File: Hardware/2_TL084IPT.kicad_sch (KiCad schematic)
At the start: 34 parts

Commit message: after merge dev
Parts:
- gave numbers to parts that had none: 30

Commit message: add R0603 footprint
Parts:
- C18: footprint (none) -> IVS_FOOTPRINTS:C0603
- R42, R43, R44, R45, R46, R47, R48, R49, R50, R51, R52, R53, R54, R55, R56, R57: footprint (none) -> IVS_FOOTPRINTS:R0603
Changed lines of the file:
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@@
       (effects (font (size 1.27 1.27)) (justify left))
     )
-    (property "Footprint" "" (id 2) (at 112.522 123.19 90)
+    (property "Footprint" "IVS_FOOTPRINTS:R0603" (id 2) (at 112.522 123.19 90)
       (effects (font (size 1.27 1.27)) hide)
     )
@@
       (effects (font (size 1.27 1.27)) (justify left))
     )
-    (property "Footprint" "" (id 2) (at 65.532 88.9 90)
+    (property "Footprint" "IVS_FOOTPRINTS:R0603" (id 2) (at 65.532 88.9 90)
       (effects (font (size 1.27 1.27)) hide)
     )
@@
       (effects (font (size 1.27 1.27)) (justify left))
     )
-    (property "Footprint" "" (id 2) (at 65.532 133.35 90)
+    (property "Footprint" "IVS_FOOTPRINTS:R0603" (id 2) (at 65.532 133.35 90)
       (effects (font (size 1.27 1.27)) hide)
     )
@@
       (effects (font (size 1.27 1.27)) (justify left))
     )
-    (property "Footprint" "" (id 2) (at 65.532 43.18 90)
+    (property "Footprint" "IVS_FOOTPRINTS:R0603" (id 2) (at 65.532 43.18 90)
       (effects (font (size 1.27 1.27)) hide)
     )
@@
       (effects (font (size 1.27 1.27)) (justify left))
     )
-    (property "Footprint" "" (id 2) (at 87.122 95.25 90)
+    (property "Footprint" "IVS_FOOTPRINTS:R0603" (id 2) (at 87.122 95.25 90)
       (effects (font (size 1.27 1.27)) hide)
     )
@@
       (effects (font (size 1.27 1.27)) (justify left))
     )
-    (property "Footprint" "" (id 2) (at 112.522 80.01 90)
+    (property "Footprint" "IVS_FOOTPRINTS:R0603" (id 2) (at 112.522 80.01 90)
       (effects (font (size 1.27 1.27)) hide)
     )
@@
       (effects (font (size 1.27 1.27)) (justify left))
     )
-    (property "Footprint" "" (id 2) (at 65.532 177.8 90)
+    (property "Footprint" "IVS_FOOTPRINTS:R0603" (id 2) (at 65.532 177.8 90)
       (effects (font (size 1.27 1.27)) hide)
     )
@@
       (effects (font (size 1.27 1.27)) (justify left))
     )
-    (property "Footprint" "" (id 2) (at 54.102 88.9 90)
+    (property "Footprint" "IVS_FOOTPRINTS:R0603" (id 2) (at 54.102 88.9 90)
       (effects (font (size 1.27 1.27)) hide)
     )
@@
       (effects (font (size 1.27 1.27)) (justify left))
     )
-    (property "Footprint" "" (id 2) (at 54.102 133.35 90)
+    (property "Footprint" "IVS_FOOTPRINTS:R0603" (id 2) (at 54.102 133.35 90)
       (effects (font (size 1.27 1.27)) hide)
     )
@@
       (effects (font (size 1.27 1.27)) (justify left))
     )
-    (property "Footprint" "" (id 2) (at 87.122 138.43 90)
+    (property "Footprint" "IVS_FOOTPRINTS:R0603" (id 2) (at 87.122 138.43 90)
       (effects (font (size 1.27 1.27)) hide)
     )
@@
       (effects (font (size 1.27 1.27)) (justify left))
     )
-    (property "Footprint" "" (id 2) (at 112.522 168.91 90)
+    (property "Footprint" "IVS_FOOTPRINTS:R0603" (id 2) (at 112.522 168.91 90)
       (effects (font (size 1.27 1.27)) hide)
     )
@@
       (effects (font (size 1.27 1.27)) (justify left))
     )
-    (property "Footprint" "" (id 2) (at 87.122 184.15 90)
+    (property "Footprint" "IVS_FOOTPRINTS:R0603" (id 2) (at 87.122 184.15 90)
       (effects (font (size 1.27 1.27)) hide)
     )
@@
       (effects (font (size 1.27 1.27)) (justify left))
     )
-    (property "Footprint" "" (id 2) (at 112.522 34.29 90)
+    (property "Footprint" "IVS_FOOTPRINTS:R0603" (id 2) (at 112.522 34.29 90)
       (effects (font (size 1.27 1.27)) hide)
     )
@@
       (effects (font (size 1.27 1.27)) (justify left))
     )
-    (property "Footprint" "" (id 2) (at 87.122 49.53 90)
+    (property "Footprint" "IVS_FOOTPRINTS:R0603" (id 2) (at 87.122 49.53 90)
       (effects (font (size 1.27 1.27)) hide)
     )
@@
       (effects (font (size 1.27 1.27)) (justify left))
     )
-    (property "Footprint" "" (id 2) (at 54.102 43.18 90)
+    (property "Footprint" "IVS_FOOTPRINTS:R0603" (id 2) (at 54.102 43.18 90)
       (effects (font (size 1.27 1.27)) hide)
     )
@@
       (effects (font (size 1.27 1.27)) (justify left))
     )
-    (property "Footprint" "" (id 2) (at 54.102 177.8 90)
+    (property "Footprint" "IVS_FOOTPRINTS:R0603" (id 2) (at 54.102 177.8 90)
       (effects (font (size 1.27 1.27)) hide)
     )
@@
       (effects (font (size 1.27 1.27)) (justify left))
     )
-    (property "Footprint" "" (id 2) (at 82.2452 30.48 0)
-      (effects (font (size 1.27 1.27)) hide)
-    )
+    (property "Footprint" "IVS_FOOTPRINTS:C0603" (id 2) (at 82.2452 30.48 0)
+      (effects (font (size 1.27 1.27)) hide)
+    )

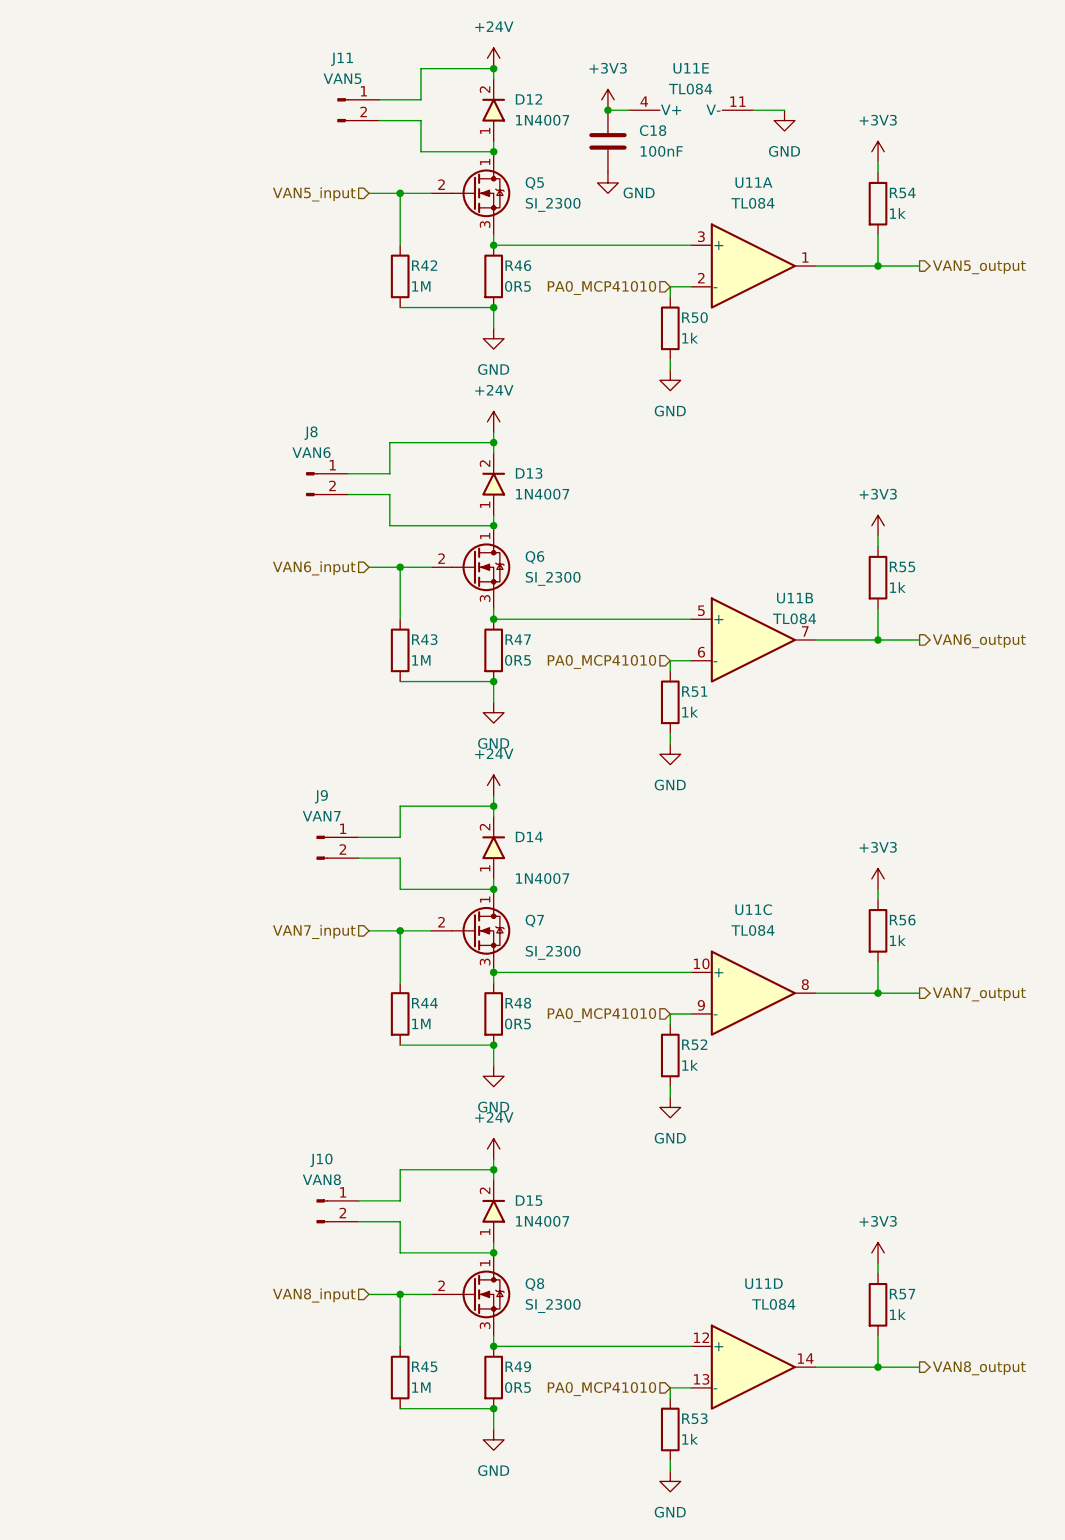
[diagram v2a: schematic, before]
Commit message: fix MCP41010, fix symbol output header
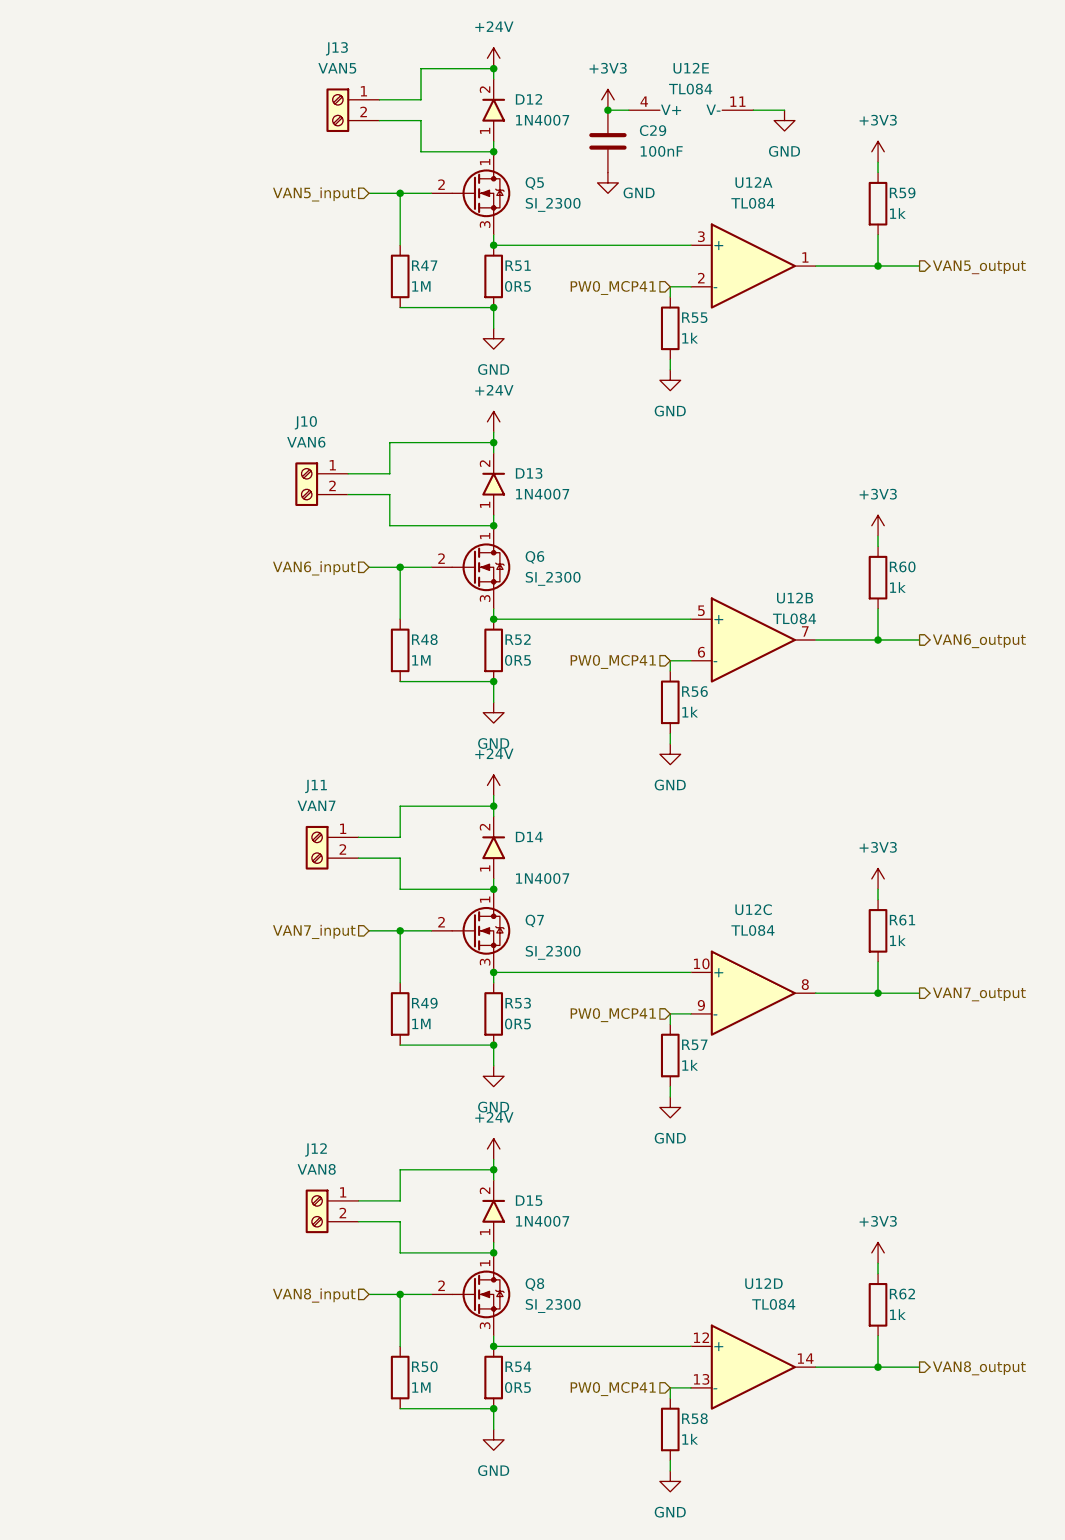
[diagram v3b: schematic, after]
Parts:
- J10: renamed from J8; symbol Connector:Conn_01x02_Male -> Connector:Screw_Terminal_01x02
- J11: renamed from J9; symbol Connector:Conn_01x02_Male -> Connector:Screw_Terminal_01x02
- J12: renamed from J10; symbol Connector:Conn_01x02_Male -> Connector:Screw_Terminal_01x02
- J13: renamed from J11; symbol Connector:Conn_01x02_Male -> Connector:Screw_Terminal_01x02
- R51: renamed from R46; footprint IVS_FOOTPRINTS:R0603 -> Resistor_SMD:R_0805_2012Metric
- R52: renamed from R47; footprint IVS_FOOTPRINTS:R0603 -> Resistor_SMD:R_0805_2012Metric
- R53: renamed from R48; footprint IVS_FOOTPRINTS:R0603 -> Resistor_SMD:R_0805_2012Metric
- R54: renamed from R49; footprint IVS_FOOTPRINTS:R0603 -> Resistor_SMD:R_0805_2012Metric
- renumbered C18 to C29, R42 to R47, R43 to R48, R44 to R49, R45 to R50, R50 to R55, R51 to R56, R52 to R57, R53 to R58, R54 to R59, R55 to R60, R56 to R61, R57 to R62, U11 to U12
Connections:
- net PA0_MCP41010 renamed PW0_MCP41

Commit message: add footprint
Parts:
- removed J10: VAN6, symbol Connector:Screw_Terminal_01x02
- removed J11: VAN7, symbol Connector:Screw_Terminal_01x02
- removed J12: VAN8, symbol Connector:Screw_Terminal_01x02
- removed J13: VAN5, symbol Connector:Screw_Terminal_01x02
- added J?: Screw_Terminal_01x08, IVS_FOOTPRINTS:HT-3.96mm, symbol Connector:Screw_Terminal_01x08
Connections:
- net +24V: now also J?.1 (Pin_1), J?.3 (Pin_3), J?.5 (Pin_5), J?.7 (Pin_7)
- net VAN5-: now reaches D12.1, Q5.1 (D)
- net VAN5-: now also J?.2 (Pin_2)
- net VAN8-: now reaches D15.1, Q8.1 (D)
- net VAN8-: now also J?.8 (Pin_8)
- net VAN6-: now reaches D13.1, Q6.1 (D)
- net VAN6-: now also J?.4 (Pin_4)
- net VAN7-: now reaches D14.1, Q7.1 (D)
- net VAN7-: now also J?.6 (Pin_6)
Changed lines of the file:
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@@
     (stroke (width 0) (type default) (color 0 0 0 0))
+  )
+  (label "VAN7+" (at 50.8 111.76 0)
+    (effects (font (size 1.27 1.27)) (justify left bottom))
+  )
+  (label "VAN5+" (at 26.67 91.44 0)
+    (effects (font (size 1.27 1.27)) (justify left bottom))
+  )
+  (label "VAN8+" (at 26.67 106.68 0)
+    (effects (font (size 1.27 1.27)) (justify left bottom))
+  )
+  (label "VAN6-" (at 26.67 99.06 0)
+    (effects (font (size 1.27 1.27)) (justify left bottom))
+  )
+  (label "VAN5-" (at 53.34 24.13 0)
+    (effects (font (size 1.27 1.27)) (justify left bottom))
+  )
+  (label "VAN8-" (at 50.8 158.75 0)
+    (effects (font (size 1.27 1.27)) (justify left bottom))
+  )
+  (label "VAN6+" (at 26.67 96.52 0)
+    (effects (font (size 1.27 1.27)) (justify left bottom))
+  )
+  (label "VAN6+" (at 49.53 67.31 0)
+    (effects (font (size 1.27 1.27)) (justify left bottom))
+  )
+  (label "VAN5-" (at 26.67 93.98 0)
+    (effects (font (size 1.27 1.27)) (justify left bottom))
+  )
+  (label "VAN7-" (at 50.8 114.3 0)
+    (effects (font (size 1.27 1.27)) (justify left bottom))
+  )
+  (label "VAN8-" (at 26.67 109.22 0)
+    (effects (font (size 1.27 1.27)) (justify left bottom))
+  )
+  (label "VAN7-" (at 26.67 104.14 0)
+    (effects (font (size 1.27 1.27)) (justify left bottom))
+  )
+  (label "VAN8+" (at 50.8 156.21 0)
+    (effects (font (size 1.27 1.27)) (justify left bottom))
+  )
+  (label "VAN5+" (at 53.34 21.59 0)
+    (effects (font (size 1.27 1.27)) (justify left bottom))
+  )
+  (label "VAN6-" (at 49.53 69.85 0)
+    (effects (font (size 1.27 1.27)) (justify left bottom))
+  )
+  (label "VAN7+" (at 26.67 101.6 0)
+    (effects (font (size 1.27 1.27)) (justify left bottom))
   )
   (hierarchical_label "VAN8_input" (shape input) (at 52.07 167.64 180)
@@
   (hierarchical_label "VAN7_output" (shape output) (at 119.38 130.81 0)
     (effects (font (size 1.27 1.27)) (justify left))
+  )
+  (symbol (lib_id "Connector:Screw_Terminal_01x08") (at 21.59 99.06 0) (mirror y) (unit 1)
+    (in_bom yes) (on_board yes) (fields_autoplaced)
+    (property "Reference" "J?" (id 0) (at 21.59 85.09 0))
+    (property "Value" "Screw_Terminal_01x08" (id 1) (at 21.59 87.63 0))
+    (property "Footprint" "IVS_FOOTPRINTS:HT-3.96mm" (id 2) (at 21.59 99.06 0)
+      (effects (font (size 1.27 1.27)) hide)
+    )
+    (property "Datasheet" "~" (id 3) (at 21.59 99.06 0)
+      (effects (font (size 1.27 1.27)) hide)
+    )
+    (pin "1")
+    (pin "2")
+    (pin "3")
+    (pin "4")
+    (pin "5")
+    (pin "6")
+    (pin "7")
+    (pin "8")
   )
   (symbol (lib_id "Amplifier_Operational:TL084") (at 99.06 41.91 0) (unit 1)
@@
     (pin "1")
   )
-  (symbol (lib_id "Connector:Screw_Terminal_01x02") (at 48.26 21.59 0) (mirror y) (unit 1)
-    (in_bom yes) (on_board yes) (fields_autoplaced)
-    (property "Reference" "J13" (id 0) (at 48.26 15.24 0))
-    (property "Value" "VAN5" (id 1) (at 48.26 17.78 0))
-    (property "Footprint" "" (id 2) (at 48.26 21.59 0)
-      (effects (font (size 1.27 1.27)) hide)
-    )
-    (property "Datasheet" "~" (id 3) (at 48.26 21.59 0)
-      (effects (font (size 1.27 1.27)) hide)
-    )
-    (pin "1")
-    (pin "2")
-  )
   (symbol (lib_id "Device:R") (at 114.3 80.01 0) (unit 1)
     (in_bom yes) (on_board yes)
@@
     (pin "2")
   )
-  (symbol (lib_id "Connector:Screw_Terminal_01x02") (at 44.45 67.31 0) (mirror y) (unit 1)
-    (in_bom yes) (on_board yes) (fields_autoplaced)
-    (property "Reference" "J10" (id 0) (at 44.45 60.96 0))
-    (property "Value" "VAN6" (id 1) (at 44.45 63.5 0))
-    (property "Footprint" "" (id 2) (at 44.45 67.31 0)
-      (effects (font (size 1.27 1.27)) hide)
-    )
-    (property "Datasheet" "~" (id 3) (at 44.45 67.31 0)
-      (effects (font (size 1.27 1.27)) hide)
-    )
-    (pin "1")
-    (pin "2")
-  )
   (symbol (lib_id "power:+3V3") (at 114.3 29.21 0) (unit 1)
     (in_bom yes) (on_board yes) (fields_autoplaced)
@@
     (pin "3")
   )
-  (symbol (lib_id "Connector:Screw_Terminal_01x02") (at 45.72 111.76 0) (mirror y) (unit 1)
-    (in_bom yes) (on_board yes) (fields_autoplaced)
-    (property "Reference" "J11" (id 0) (at 45.72 105.41 0))
-    (property "Value" "VAN7" (id 1) (at 45.72 107.95 0))
-    (property "Footprint" "" (id 2) (at 45.72 111.76 0)
-      (effects (font (size 1.27 1.27)) hide)
-    )
-    (property "Datasheet" "~" (id 3) (at 45.72 111.76 0)
-      (effects (font (size 1.27 1.27)) hide)
-    )
-    (pin "1")
-    (pin "2")
-  )
   (symbol (lib_id "Device:R") (at 55.88 43.18 0) (unit 1)
     (in_bom yes) (on_board yes)
@@
     (pin "1")
   )
-  (symbol (lib_id "Connector:Screw_Terminal_01x02") (at 45.72 156.21 0) (mirror y) (unit 1)
-    (in_bom yes) (on_board yes) (fields_autoplaced)
-    (property "Reference" "J12" (id 0) (at 45.72 149.86 0))
-    (property "Value" "VAN8" (id 1) (at 45.72 152.4 0))
-    (property "Footprint" "" (id 2) (at 45.72 156.21 0)
-      (effects (font (size 1.27 1.27)) hide)
-    )
-    (property "Datasheet" "~" (id 3) (at 45.72 156.21 0)
-      (effects (font (size 1.27 1.27)) hide)
-    )
-    (pin "1")
-    (pin "2")
-  )
   (symbol (lib_id "power:GND") (at 67.31 184.15 0) (unit 1)
